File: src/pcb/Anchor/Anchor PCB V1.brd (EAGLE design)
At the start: 100.1 x 68.7 mm, 89 parts, among them IC1 ENC28J60-I_SS, IC2 TPS23750PWP, IC3 MIC5219-3.3YM5-TR, IC4 DWM1000, J1 0826-1X1T-GJ-F, J2 105017-0001, Q1 32 MHz, Q2 SUD06N10-225L, U1 ATSAMD21G-A, Y1 25 MHz

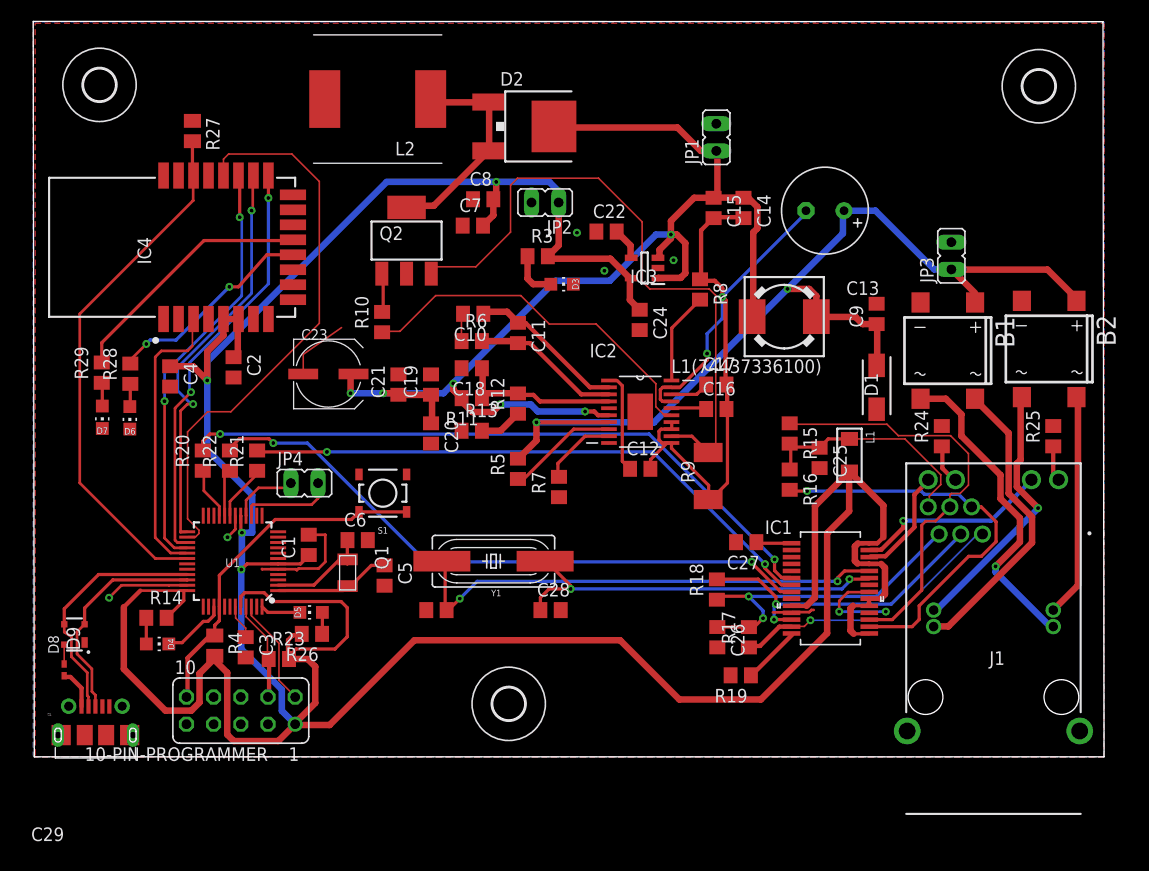
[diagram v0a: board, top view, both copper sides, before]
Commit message: Changes wiring and added forgotten connections
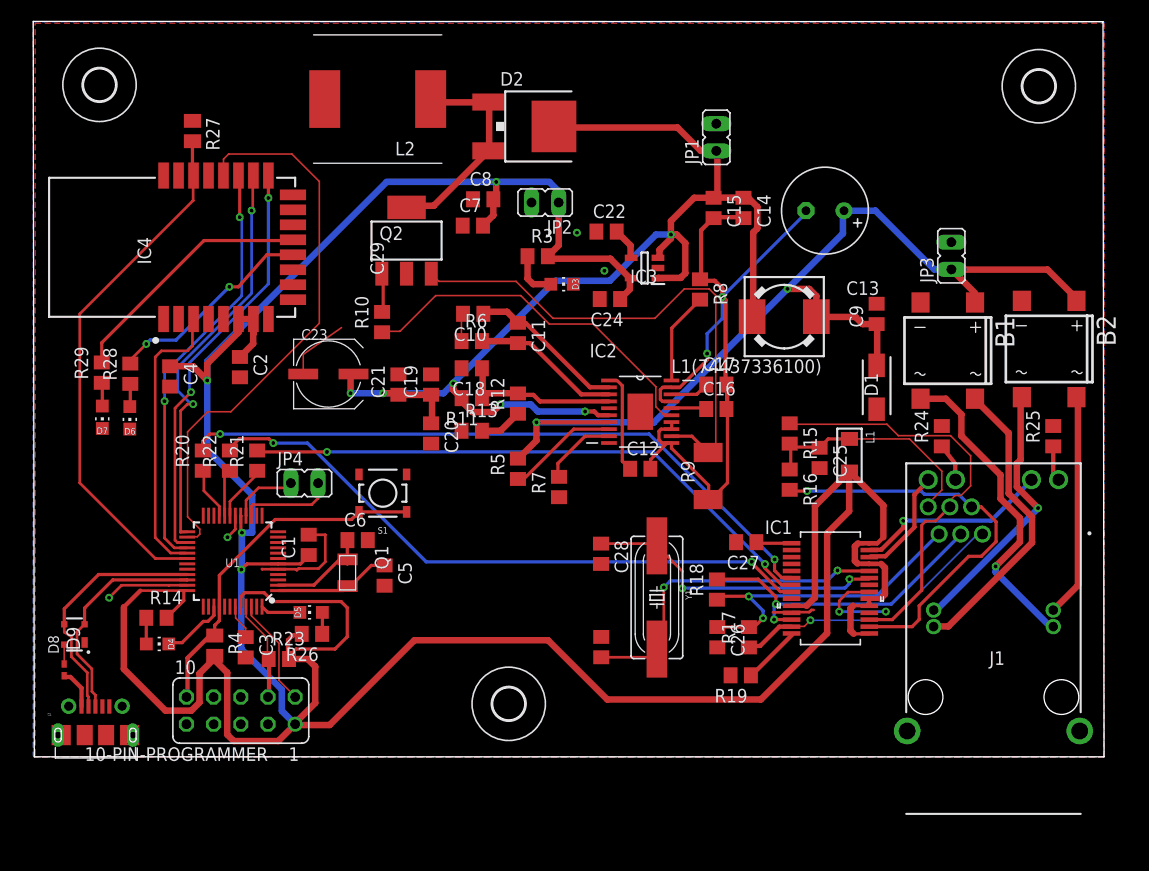
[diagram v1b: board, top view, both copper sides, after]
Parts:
- moved C29 15.8 mm to (53.0, 10.3), turned to 90 degrees
- moved Y1 15.6 mm to (58.2, 14.9), turned to 270 degrees
- moved C28 7.07 mm to (53.0, 19.0), turned to 270 degrees
- moved C24 3.40 mm to (53.8, 42.8), turned to 180 degrees
- moved C2 0.60 mm to (19.2, 36.4)
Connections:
- net VCC: now also IC4.7; no longer IC4.5
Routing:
- net OSC2: track 46.1 -> 31.6 mm
- net RSP: track 59.8 -> 49.6 mm
- net OSC1: track 36.5 -> 28.4 mm
- net VCC: track 319.0 -> 319.5 mm
- net GND: vias 7 -> 6

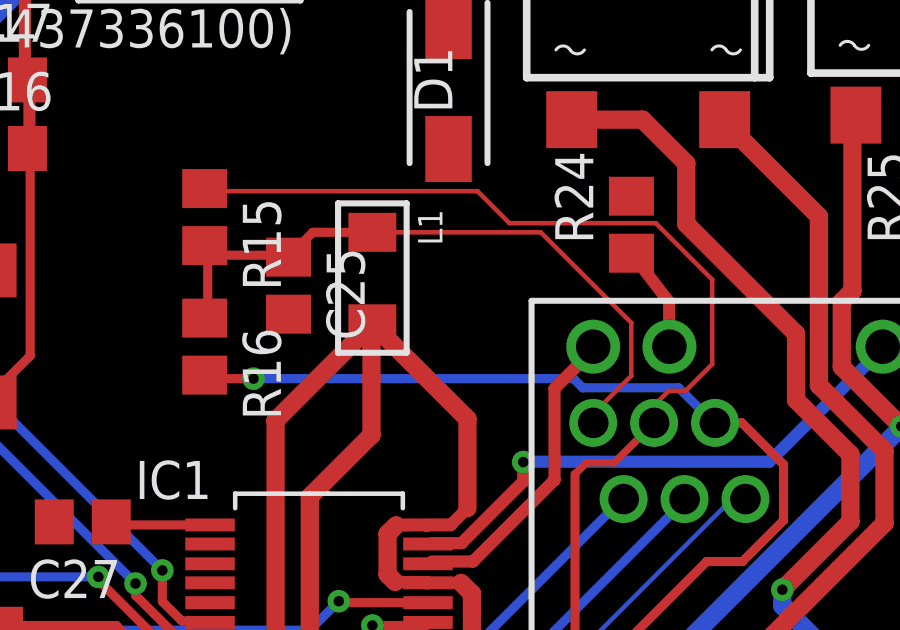
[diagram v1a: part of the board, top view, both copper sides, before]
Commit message: V2 Updaten mistakes
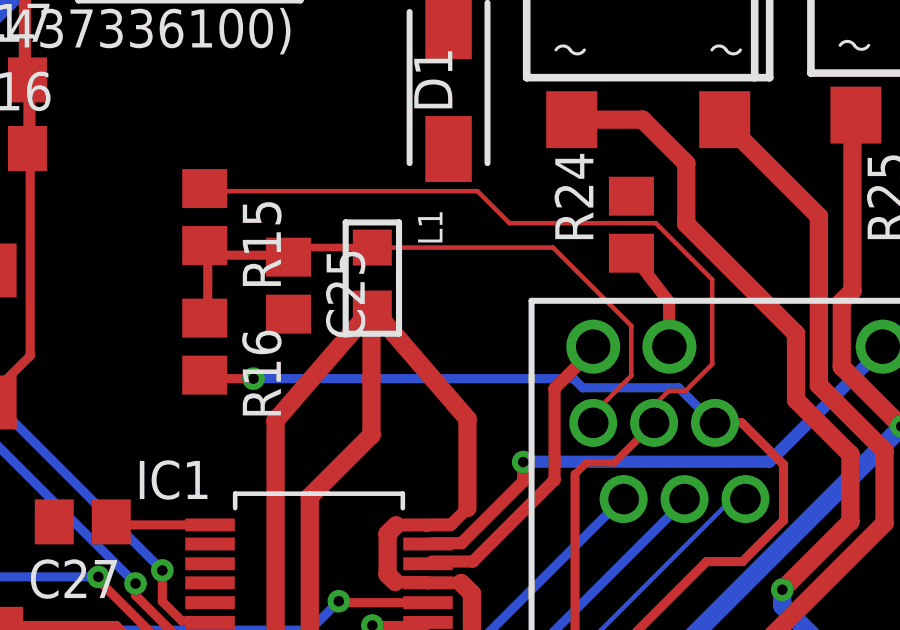
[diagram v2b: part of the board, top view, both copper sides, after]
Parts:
- L1: value FB_1206 -> FB_0805; device rc-master-smd:L1206 -> rc-master-smd:L0805
- R9: value 0.18 mΩ (0.5W) -> 0.18 Ω (0.5W)
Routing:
- net VCC: track 319.5 -> 320.7 mm
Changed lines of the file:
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@@
 <attribute name="VALUE" x="62.484" y="32.258" size="1.27" layer="27"/>
 </element>
-<element name="R9" library="rcl" library_urn="urn:adsk.eagle:library:334" package="R2010" package3d_urn="urn:adsk.eagle:package:23551/2" value="0.18 mΩ (0.5W)" x="62.992" y="26.248" smashed="yes" rot="R90">
+<element name="R9" library="rcl" library_urn="urn:adsk.eagle:library:334" package="R2010" package3d_urn="urn:adsk.eagle:package:23551/2" value="0.18 Ω (0.5W)" x="62.992" y="26.248" smashed="yes" rot="R90">
 <attribute name="NAME" x="61.722" y="25.613" size="1.27" layer="25" rot="R90"/>
 <attribute name="SPICEPREFIX" value="R" x="62.992" y="26.248" size="1.778" layer="27" rot="R90" display="off"/>
@@
 <attribute name="VALUE" x="61.307978125" y="12.45361875" size="1.27" layer="27" rot="R270"/>
 </element>
-<element name="L1" library="rc-master-smd" package="L1206" value="FB_1206" x="76.2" y="28.194" smashed="yes" rot="R270">
+<element name="L1" library="rc-master-smd" package="L0805" value="FB_0805" x="76.2" y="28.194" smashed="yes" rot="R270">
 <attribute name="NAME" x="77.724" y="30.48" size="0.8128" layer="25" ratio="18" rot="R270"/>
 <attribute name="VALUE" x="80.772" y="27.94" size="0.6096" layer="27" ratio="10" rot="R270"/>
@@
 <wire x1="78.0288" y1="14.7828" x2="78.0542" y2="14.7828" width="0.4064" layer="1"/>
 <wire x1="78.0288" y1="14.1732" x2="78.0542" y2="14.1224" width="0.4064" layer="1"/>
-<wire x1="76.2" y1="26.67" x2="79.369921875" y2="23.500078125" width="0.6096" layer="1"/>
+<wire x1="76.2" y1="27.178" x2="79.369921875" y2="23.500078125" width="0.6096" layer="1"/>
 <wire x1="79.369921875" y1="23.500078125" x2="79.369921875" y2="20.520665625" width="0.6096" layer="1"/>
 <wire x1="79.369921875" y1="20.520665625" x2="78.81365625" y2="19.9644" width="0.4064" layer="1"/>
@@
 <wire x1="72.9742" y1="14.89201875" x2="72.19188125" y2="14.1097" width="0.6096" layer="1"/>
 <wire x1="72.9742" y1="23.4442" x2="72.9742" y2="14.89201875" width="0.6096" layer="1"/>
-<wire x1="76.2" y1="26.67" x2="72.9742" y2="23.4442" width="0.6096" layer="1"/>
+<wire x1="76.2" y1="27.178" x2="72.9742" y2="23.4442" width="0.6096" layer="1"/>
 <wire x1="79.1083" y1="14.7828" x2="78.0542" y2="14.7828" width="0.4064" layer="1"/>
 <wire x1="79.519778125" y1="15.194278125" x2="79.1083" y2="14.7828" width="0.6096" layer="1"/>
@@
 <wire x1="76.296521875" y1="11.795759375" x2="76.296521875" y2="13.883640625" width="0.6096" layer="1"/>
 <wire x1="76.172059375" y1="22.9641375" x2="76.172059375" y2="26.642059375" width="0.6096" layer="1"/>
-<wire x1="76.172059375" y1="26.642059375" x2="76.2" y2="26.67" width="0.6096" layer="1"/>
+<wire x1="76.172059375" y1="26.642059375" x2="76.2" y2="27.178" width="0.6096" layer="1"/>
 <wire x1="16.8681375" y1="9.4386" x2="16.8681375" y2="9.217621875" width="0.6096" layer="1"/>
 <wire x1="16.8681375" y1="9.217621875" x2="15.4432" y2="7.792684375" width="0.6096" layer="1"/>
@@
 <wire x1="73.3044" y1="28.956" x2="73.406" y2="28.89" width="0.1524" layer="1"/>
 <wire x1="70.7136" y1="28.956" x2="70.612" y2="29.276" width="0.1524" layer="1"/>
-<wire x1="74.2188" y1="29.718" x2="76.2" y2="29.718" width="0.3048" layer="1"/>
-<wire x1="73.4568" y1="28.956" x2="74.2188" y2="29.718" width="0.3048" layer="1"/>
 <wire x1="73.4568" y1="28.956" x2="73.406" y2="28.89" width="0.1524" layer="1"/>
 <wire x1="83.6676" y1="23.771859375" x2="83.6676" y2="23.4696" width="0.1524" layer="1"/>
 <wire x1="84.830921875" y1="24.93518125" x2="83.6676" y2="23.771859375" width="0.1524" layer="1"/>
-<wire x1="84.830921875" y1="26.703021875" x2="84.830921875" y2="24.93518125" width="0.1524" layer="1"/>
-<wire x1="81.81594375" y1="29.718" x2="84.830921875" y2="26.703021875" width="0.1524" layer="1"/>
-<wire x1="76.2" y1="29.718" x2="81.81594375" y2="29.718" width="0.1524" layer="1"/>
+<wire x1="84.830921875" y1="24.93518125" x2="84.830921875" y2="26.601421875" width="0.1524" layer="1"/>
 <wire x1="83.6676" y1="23.4696" x2="83.562" y2="23.366" width="0.1524" layer="1"/>
+<wire x1="84.830921875" y1="26.601421875" x2="82.22234375" y2="29.21" width="0.1524" layer="1"/>
+<wire x1="82.22234375" y1="29.21" x2="76.2" y2="29.21" width="0.1524" layer="1"/>
+<wire x1="76.2" y1="29.21" x2="73.726" y2="29.21" width="0.254" layer="1"/>
+<wire x1="73.726" y1="29.21" x2="73.406" y2="28.89" width="0.254" layer="1"/>
 </signal>
 <signal name="N$6">
